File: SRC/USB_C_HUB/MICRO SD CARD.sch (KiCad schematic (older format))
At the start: 20 parts

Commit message: all but HDMI and UFP PD
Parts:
- removed J?: SD_Card, symbol Connector:SD_Card
- added J?: Micro_SD_Card_Det, symbol Connector:Micro_SD_Card_Det
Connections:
- net CRD_PWR: now also J?.4 (VDD)
- net GND: now also J?.11 (SHIELD), J?.6 (VSS)
- net SD_CD: now also J?.10 (DET_A)
- net SD_CLK: now also J?.5 (CLK)
- net SD_CMD: now also J?.3 (CMD)
- net SD_D0: now also J?.7 (DAT0)
- net SD_D1: now also J?.8 (DAT1)
- net SD_D2: now also J?.1 (DAT2)
- net SD_D3: now also J?.2 (DAT3/CD)
- net SD_WP: no longer names the net of IC?.30 (XD_D4_/_GPIO6_(SD_WP)_/_MS_SCLK)
- no-connect marks 13 -> 15
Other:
- note added: "Detect"
- moved on the sheet: C?
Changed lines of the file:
@@
 $Descr A4 11693 8268
 encoding utf-8
-Sheet 6 11
+Sheet 9 11
 Title ""
 Date ""
@@
 Comment4 ""
 $EndDescr
-Text Label 10725 3325 0    50   ~ 0
-SD_CD
 $Comp
 L OLIMEX_Power:GND #PWR?
 U 1 1 63D3BD81
-P 10775 3700
+P 10575 4100
 AR Path="/619540C6/63D3BD81" Ref="#PWR?"  Part="1"
 AR Path="/63D3BD81" Ref="#PWR?"  Part="1"
 AR Path="/63D2BAD4/63D3BD81" Ref="#PWR?"  Part="1"
 AR Path="/66525694/63D3BD81" Ref="#PWR?"  Part="1"
-F 0 "#PWR?" H 10775 3450 50  0001 C CNN
-F 1 "GND" H 10780 3527 50  0000 C CNN
-F 2 "" H 10775 3700 60  0000 C CNN
-F 3 "" H 10775 3700 60  0000 C CNN
-	1    10775 3700
+F 0 "#PWR?" H 10575 3850 50  0001 C CNN
+F 1 "GND" H 10580 3927 50  0000 C CNN
+F 2 "" H 10575 4100 60  0000 C CNN
+F 3 "" H 10575 4100 60  0000 C CNN
+	1    10575 4100
 	-1   0    0    -1
 $EndComp
 Wire Wire Line
-	10775 3625 10775 3700
-Text Label 10750 3425 0    50   ~ 0
-SD_WP
-Wire Wire Line
-	10750 3425 10550 3425
-Wire Wire Line
-	10650 3625 10775 3625
-Connection ~ 10650 3625
+	10575 4025 10575 4100
+Wire Wire Line
+	10450 4025 10575 4025
 Wire Wire Line
 	10650 3725 10650 3625
-Wire Wire Line
-	10550 3725 10650 3725
-Wire Wire Line
-	10550 3625 10650 3625
-Wire Wire Line
-	10550 3325 10725 3325
 NoConn ~ 6300 2625
 NoConn ~ 6300 2775
@@
 Wire Wire Line
 	6525 3525 6350 3525
-Text Label 6525 3525 0    50   ~ 0
-SD_WP
-Wire Wire Line
-	8050 3725 8750 3725
-Connection ~ 7800 3725
-Wire Wire Line
-	7800 3725 8050 3725
-Wire Wire Line
-	7800 3675 7800 3725
 $Comp
 L Device:C_Small C?
 U 1 1 63D332FA
-P 7800 3575
+P 7875 3625
 AR Path="/63D332FA" Ref="C?"  Part="1"
 AR Path="/63D2BAD4/63D332FA" Ref="C?"  Part="1"
 AR Path="/66525694/63D332FA" Ref="C?"  Part="1"
-F 0 "C?" H 7892 3621 50  0000 L CNN
-F 1 "1nF" H 7892 3530 50  0000 L CNN
-F 2 "" H 7800 3575 50  0001 C CNN
-F 3 "~" H 7800 3575 50  0001 C CNN
-	1    7800 3575
-	1    0    0    -1
-$EndComp
-Text Label 7800 3375 2    31   ~ 0
+F 0 "C?" H 7967 3671 50  0000 L CNN
+F 1 "1nF" H 7967 3580 50  0000 L CNN
+F 2 "" H 7875 3625 50  0001 C CNN
+F 3 "~" H 7875 3625 50  0001 C CNN
+	1    7875 3625
+	1    0    0    -1
+$EndComp
+Text Label 7875 3425 2    31   ~ 0
 CRD_PWR
-Connection ~ 8050 3725
-Wire Wire Line
-	8050 3425 8750 3425
-Wire Wire Line
-	8050 3725 8050 3425
 $Comp
 L OLIMEX_Power:GND #PWR?
 U 1 1 63D332F0
-P 7800 3725
+P 7875 3775
 AR Path="/619540C6/63D332F0" Ref="#PWR?"  Part="1"
 AR Path="/63D332F0" Ref="#PWR?"  Part="1"
 AR Path="/63D2BAD4/63D332F0" Ref="#PWR?"  Part="1"
 AR Path="/66525694/63D332F0" Ref="#PWR?"  Part="1"
-F 0 "#PWR?" H 7800 3475 50  0001 C CNN
-F 1 "GND" H 7805 3552 50  0000 C CNN
-F 2 "" H 7800 3725 60  0000 C CNN
-F 3 "" H 7800 3725 60  0000 C CNN
-	1    7800 3725
+F 0 "#PWR?" H 7875 3525 50  0001 C CNN
+F 1 "GND" H 7880 3602 50  0000 C CNN
+F 2 "" H 7875 3775 60  0000 C CNN
+F 3 "" H 7875 3775 60  0000 C CNN
+	1    7875 3775
 	-1   0    0    -1
 $EndComp
@@
 SD_CLK
 Wire Wire Line
-	8750 3625 8575 3625
-Text Label 8575 3625 2    50   ~ 0
+	8750 3525 8575 3525
+Text Label 8575 3525 2    50   ~ 0
 SD_CLK
 Wire Wire Line
@@
 SD_CMD
 Wire Wire Line
-	8575 3925 8750 3925
-Wire Wire Line
 	8575 3825 8750 3825
+Wire Wire Line
+	8575 3725 8750 3725
 Wire Wire Line
 	8575 3225 8750 3225
@@
 Text Label 8575 3125 2    50   ~ 0
 SD_D2
-Text Label 8575 3925 2    50   ~ 0
+Text Label 8575 3825 2    50   ~ 0
 SD_D1
-Text Label 8575 3825 2    50   ~ 0
+Text Label 8575 3725 2    50   ~ 0
 SD_D0
 Text Label 6525 3725 0    50   ~ 0
@@
 Text Label 6525 3325 0    50   ~ 0
 SD_D0
-$Comp
-L Connector:SD_Card J?
-U 1 1 63D332CA
-P 9650 3525
-AR Path="/63D332CA" Ref="J?"  Part="1"
-AR Path="/63D2BAD4/63D332CA" Ref="J?"  Part="1"
-AR Path="/66525694/63D332CA" Ref="J?"  Part="1"
-F 0 "J?" H 9650 4190 50  0000 C CNN
-F 1 "SD_Card" H 9650 4099 50  0000 C CNN
-F 2 "" H 9650 3525 50  0001 C CNN
-F 3 "http://portal.fciconnect.com/Comergent//fci/drawing/10067847.pdf" H 9650 3525 50  0001 C CNN
-	1    9650 3525
-	1    0    0    -1
-$EndComp
 Wire Wire Line
 	8550 2625 8900 2625
@@
 Wire Wire Line
 	2175 4050 2375 4050
+Wire Wire Line
+	7875 3425 7875 3525
+Text Label 8550 3425 2    31   ~ 0
+CRD_PWR
+Wire Wire Line
+	8750 3425 8550 3425
+Text Notes 5150 775  0    39   ~ 0
+DECOUPLING CAPS
+$Comp
+L Connector:Micro_SD_Card_Det J?
+U 1 1 66574B47
+P 9650 3525
+F 0 "J?" H 9600 4342 50  0000 C CNN
+F 1 "Micro_SD_Card_Det" H 9600 4251 50  0000 C CNN
+F 2 "" H 11700 4225 50  0001 C CNN
+F 3 "https://www.hirose.com/product/en/download_file/key_name/DM3/category/Catalog/doc_file_id/49662/?file_category_id=4&item_id=195&is_series=1" H 9650 3625 50  0001 C CNN
+	1    9650 3525
+	1    0    0    -1
+$EndComp
+Wire Wire Line
+	7875 3775 7875 3750
+Wire Wire Line
+	8750 3625 8200 3625
+Wire Wire Line
+	8200 3625 8200 3750
+Wire Wire Line
+	8200 3750 7875 3750
+Connection ~ 7875 3750
+Wire Wire Line
+	7875 3750 7875 3725
+NoConn ~ 8750 4025
 $Comp
 L SamacSys_Parts:USB2240-AEZG-06 IC?
@@
 $EndComp
 Wire Wire Line
-	7800 3375 7800 3475
-Text Label 8550 3525 2    31   ~ 0
-CRD_PWR
-Wire Wire Line
-	8750 3525 8550 3525
-Text Notes 5150 775  0    39   ~ 0
-DECOUPLING CAPS
+	10550 3625 10650 3625
+Wire Wire Line
+	10550 3725 10650 3725
+NoConn ~ 6525 3525
+Text Label 8575 3925 2    50   ~ 0
+SD_CD
+Wire Wire Line
+	8750 3925 8575 3925
+Text Notes 6825 2950 2    20   ~ 0
+Detect
 $EndSCHEMATC

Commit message: ALL DONE BUT THE HDMI SECTION. NEED FOOTPRINT ASSIGNMENT
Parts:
- removed C? (x2): 0.1uF, symbol Device:C_Small
- removed C?: 4.7uF, symbol Device:C_Small
- removed C?: 1nF, symbol Device:C_Small
- removed IC?: USB2240-AEZG-06, QFN50P600X600X100-37N-D, symbol SamacSys_Parts:USB2240-AEZG-06
- removed Y?: 24.0MHz, symbol Device:Crystal_GND24_Small
- added C69: 4.7uF, symbol Device:C_Small
- added C72, C73: 0.1uF, symbol Device:C_Small
- added C74: 1nF, symbol Device:C_Small
- added IC4: USB2240-AEZG-06, SamacSys_Parts_2:QFN50P600X600X100-37N-D, symbol SamacSys_Parts:USB2240-AEZG-06
- added Y3: 24.0MHz, symbol Device:Crystal_GND24_Small
- gave numbers to parts that had none: 14
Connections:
- net +3V3: now also C69.1, C72.1, C73.1, IC4.14 (VDD33_2), IC4.22 (VDD33_3), IC4.36 (VDDA33), IC4.6 (VDD33_1)
- net CRD_PWR: now also C74.1, IC4.21 (GPIO10_(CRD_PWR))
- net GND: now also C69.2, C72.2, C73.2, C74.2, IC4.28 (TEST), IC4.37 (GND), Y3.2, Y3.4
- net SD_CD: now also IC4.26 (GPIO15_(SD_NCD))
- net SD_CLK: now also IC4.9 (XD_NWP_/_SD_CLK_/_MS_BS)
- net SD_CMD: now also IC4.11 (XD_CLE_/_SD_CMD_/_MS_D0)
- net SD_D0: now also IC4.5 (XD_D2_/_SD_D0_/_MS_D4)
- net SD_D1: now also IC4.4 (XD_D3_/_SD_D1_/_MS_D5)
- net SD_D2: now also IC4.25 (XD_D5_/_SD_D2)
- net SD_D3: now also IC4.23 (XD_D6_/_SD_D3_/_MS_D3)
- net USB+: now also IC4.2 (USB+)
- net USB-: now also IC4.3 (USB-)
- net XTAL1: now also IC4.33 (XTAL1_(CLKIN)), Y3.1
- net XTAL2: now also IC4.32 (XTAL2), Y3.3
- net at R56.2: now also IC4.18 (RESET_N)
- net at C67.1: now also IC4.34 (VDD18PLL)
- net at C68.1: now also IC4.13 (VDD18)
- net at R57.1: now also IC4.35 (RBIAS)
- net at R58.2: now also IC4.29 (GPIO4)

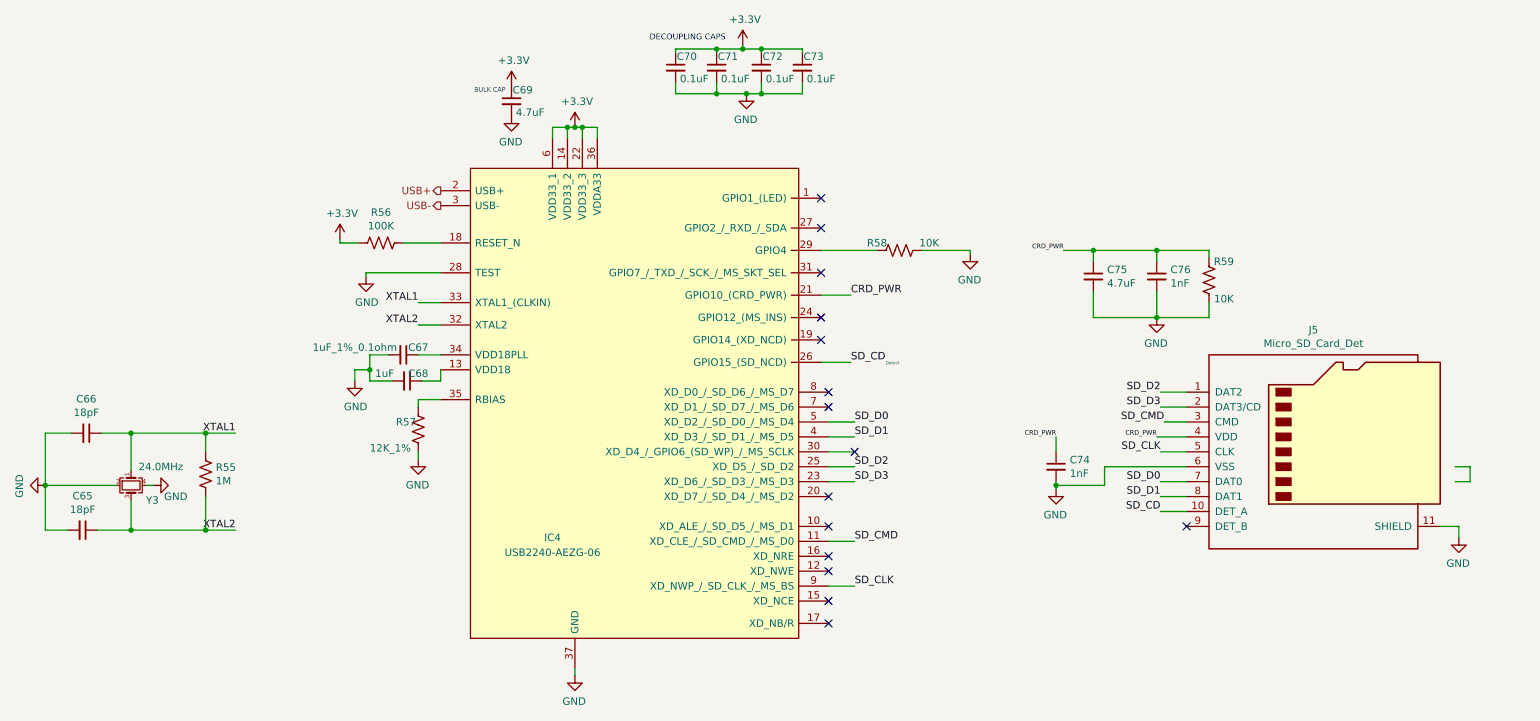
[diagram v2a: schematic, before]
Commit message: schematic capture complete. Pending Footprint assignment. accetable Errors=21
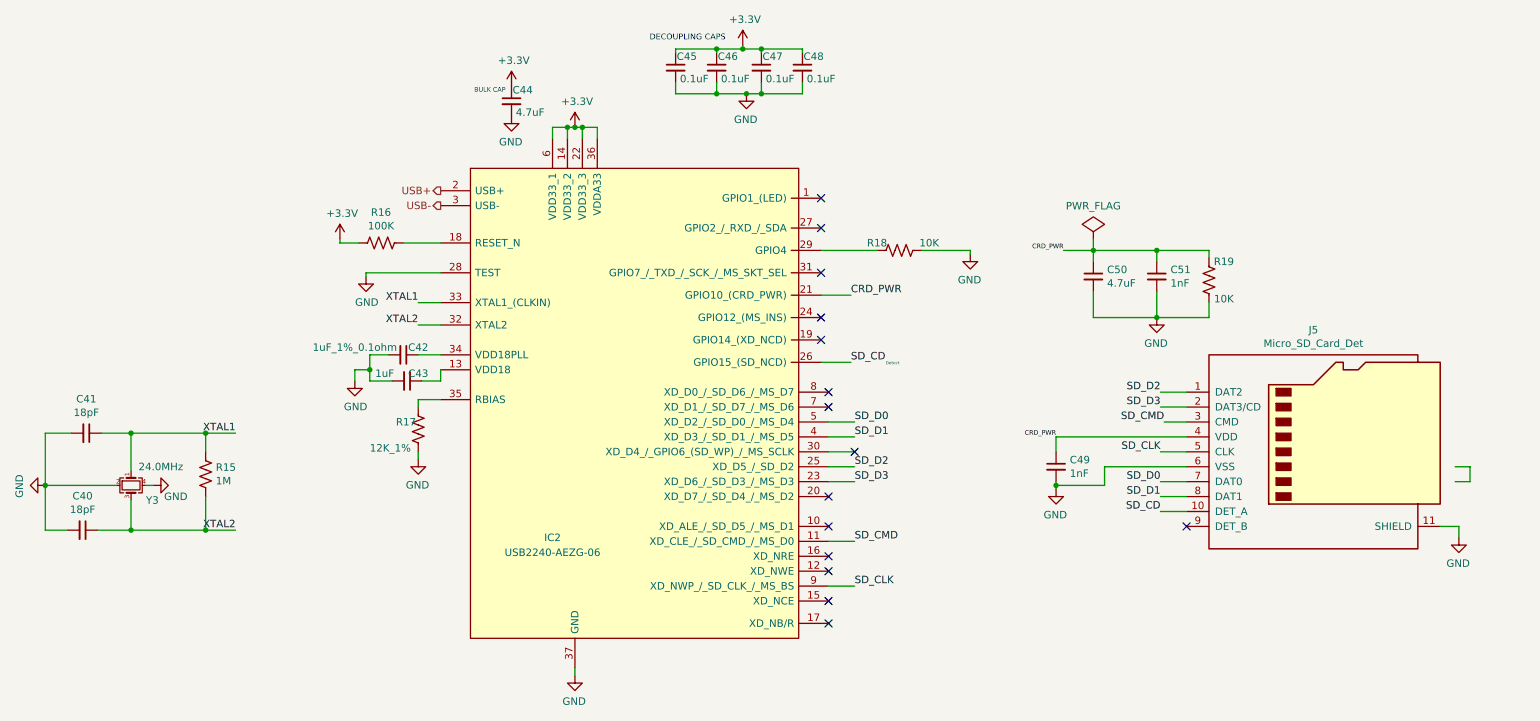
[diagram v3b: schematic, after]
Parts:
- renumbered C65 to C40, C66 to C41, C67 to C42, C68 to C43, C69 to C44, C70 to C45, C71 to C46, C72 to C47, C73 to C48, C74 to C49, C75 to C50, C76 to C51, IC4 to IC2, R55 to R15, R56 to R16, R57 to R17, R58 to R18, R59 to R19

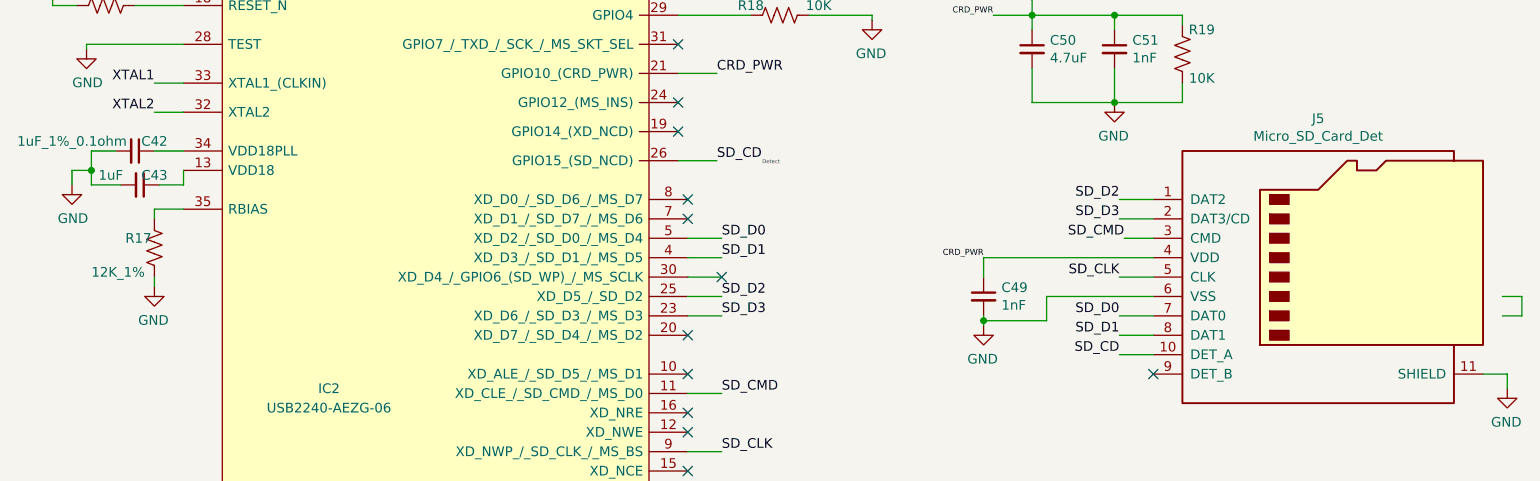
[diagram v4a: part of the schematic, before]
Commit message: schematic capture and footprint assignment complete. Pending approval
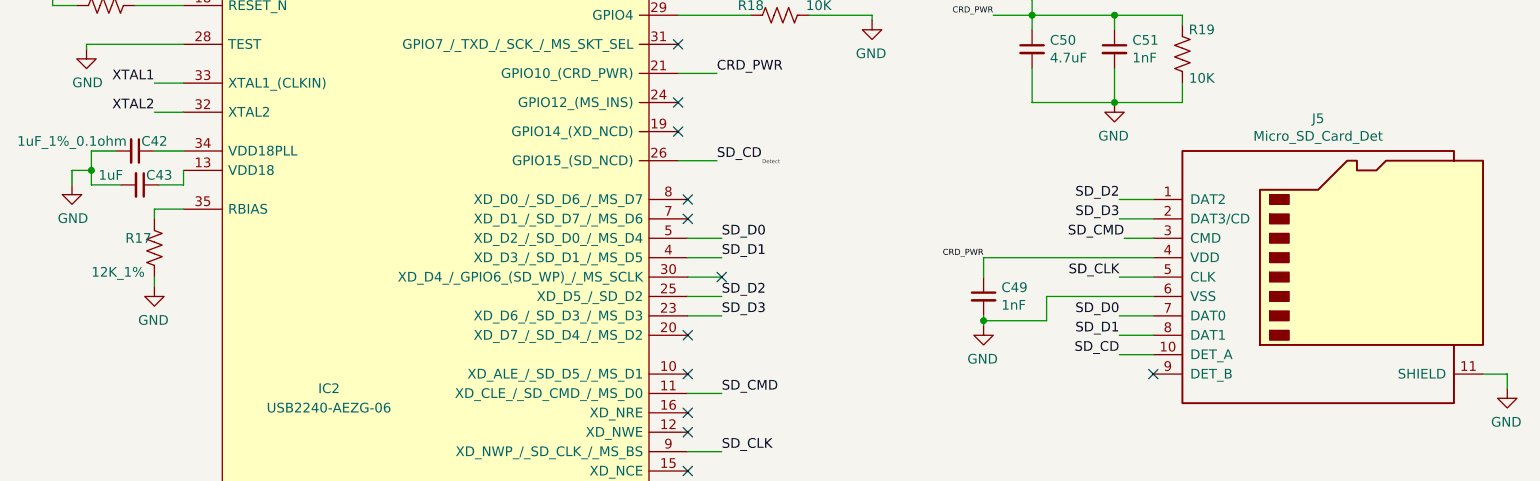
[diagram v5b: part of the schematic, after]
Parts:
- C40, C41, C45, C46, C47, C48: footprint (none) -> Capacitor_SMD:C_0402_1005Metric
- C42, C43: footprint (none) -> Capacitor_SMD:C_0603_1608Metric; Mfr No. (none) -> GMC10X7R105J16NT; Vendor (none) -> DK
- C44, C50: footprint (none) -> Capacitor_SMD:C_0603_1608Metric; Mfr No. (none) -> CL10A475KQ8NNNC
- C49, C51: footprint (none) -> Capacitor_SMD:C_0402_1005Metric; Mfr No. (none) -> C0402C102J1GEC7411
- J5: footprint (none) -> footprints:GCT_MEM2051-00-195-00-A
- R15, R18, R19: footprint (none) -> Resistor_SMD:R_0402_1005Metric
- R16: footprint (none) -> Resistor_SMD:R_0402_1005Metric; Mfr No. (none) -> 0402WGF1003TCE
- R17: footprint (none) -> Resistor_SMD:R_0402_1005Metric; Mfr No. (none) -> RTT021202FTH
- Y3: footprint (none) -> Crystal:Crystal_SMD_2016-4Pin_2.0x1.6mm; Mfr No. (none) -> ABM11-24.000MHZ-D2X-T3
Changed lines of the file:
@@
 Wire Wire Line
 	10450 4025 10575 4025
-Wire Wire Line
-	10650 3725 10650 3625
 NoConn ~ 6300 2625
 NoConn ~ 6300 2775
@@
 F 0 "C49" H 7967 3671 50  0000 L CNN
 F 1 "1nF" H 7967 3580 50  0000 L CNN
-F 2 "" H 7875 3625 50  0001 C CNN
+F 2 "Capacitor_SMD:C_0402_1005Metric" H 7875 3625 50  0001 C CNN
 F 3 "~" H 7875 3625 50  0001 C CNN
+F 4 "C0402C102J1GEC7411" H 7875 3625 50  0001 C CNN "Mfr No."
 	1    7875 3625
 	1    0    0    -1
@@
 F 0 "R19" H 8800 2250 50  0000 C CNN
 F 1 "10K" H 8800 2500 50  0000 C CNN
-F 2 "" V 8940 2365 50  0001 C CNN
+F 2 "Resistor_SMD:R_0402_1005Metric" V 8940 2365 50  0001 C CNN
 F 3 "~" H 8900 2375 50  0001 C CNN
 	1    8900 2375
@@
 F 0 "C51" H 8642 2396 50  0000 L CNN
 F 1 "1nF" H 8642 2305 50  0000 L CNN
-F 2 "" H 8550 2350 50  0001 C CNN
+F 2 "Capacitor_SMD:C_0402_1005Metric" H 8550 2350 50  0001 C CNN
 F 3 "~" H 8550 2350 50  0001 C CNN
+F 4 "C0402C102J1GEC7411" H 8550 2350 50  0001 C CNN "Mfr No."
 	1    8550 2350
 	1    0    0    -1
@@
 F 0 "C50" H 8217 2396 50  0000 L CNN
 F 1 "4.7uF" H 8217 2305 50  0000 L CNN
-F 2 "" H 8125 2350 50  0001 C CNN
+F 2 "Capacitor_SMD:C_0603_1608Metric" H 8125 2350 50  0001 C CNN
 F 3 "~" H 8125 2350 50  0001 C CNN
+F 4 "CL10A475KQ8NNNC" H 8125 2350 50  0001 C CNN "Mfr No."
 	1    8125 2350
 	1    0    0    -1
@@
 F 0 "R18" V 6775 2025 50  0000 C CNN
 F 1 "10K" V 6775 2375 50  0000 C CNN
-F 2 "" V 6865 2165 50  0001 C CNN
+F 2 "Resistor_SMD:R_0402_1005Metric" V 6865 2165 50  0001 C CNN
 F 3 "~" H 6825 2175 50  0001 C CNN
 	1    6825 2175
@@
 F 0 "R17" H 3450 3425 50  0000 L CNN
 F 1 "12K_1%" H 3275 3250 50  0000 L CNN
-F 2 "" V 3640 3365 50  0001 C CNN
+F 2 "Resistor_SMD:R_0402_1005Metric" V 3640 3365 50  0001 C CNN
 F 3 "~" H 3600 3375 50  0001 C CNN
+F 4 "RTT021202FTH" H 3600 3375 50  0001 C CNN "Mfr No."
 	1    3600 3375
 	1    0    0    -1
@@
 AR Path="/63D2BAD4/642D7819" Ref="C?"  Part="1"
 AR Path="/66525694/642D7819" Ref="C44"  Part="1"
+AR Path="/6609E24E/642D7819" Ref="C44"  Part="1"
 F 0 "C44" H 4300 1250 50  0000 C CNN
 F 1 "4.7uF" H 4350 1100 50  0000 C CNN
-F 2 "" H 4225 1175 50  0001 C CNN
+F 2 "Capacitor_SMD:C_0603_1608Metric" H 4225 1175 50  0001 C CNN
 F 3 "~" H 4225 1175 50  0001 C CNN
+F 4 "CL10A475KQ8NNNC" H 4225 1175 50  0001 C CNN "Mfr No."
 	1    4225 1175
 	1    0    0    -1
@@
 F 0 "C48" H 6250 1025 50  0000 C CNN
 F 1 "0.1uF" H 6300 875 50  0000 C CNN
-F 2 "" H 6175 950 50  0001 C CNN
+F 2 "Capacitor_SMD:C_0402_1005Metric" H 6175 950 50  0001 C CNN
 F 3 "~" H 6175 950 50  0001 C CNN
 	1    6175 950
@@
 F 0 "C47" H 5975 1025 50  0000 C CNN
 F 1 "0.1uF" H 6025 875 50  0000 C CNN
-F 2 "" H 5900 950 50  0001 C CNN
+F 2 "Capacitor_SMD:C_0402_1005Metric" H 5900 950 50  0001 C CNN
 F 3 "~" H 5900 950 50  0001 C CNN
 	1    5900 950
@@
 F 0 "C46" H 5675 1025 50  0000 C CNN
 F 1 "0.1uF" H 5725 875 50  0000 C CNN
-F 2 "" H 5600 950 50  0001 C CNN
+F 2 "Capacitor_SMD:C_0402_1005Metric" H 5600 950 50  0001 C CNN
 F 3 "~" H 5600 950 50  0001 C CNN
 	1    5600 950
@@
 F 0 "C45" H 5400 1025 50  0000 C CNN
 F 1 "0.1uF" H 5450 875 50  0000 C CNN
-F 2 "" H 5325 950 50  0001 C CNN
+F 2 "Capacitor_SMD:C_0402_1005Metric" H 5325 950 50  0001 C CNN
 F 3 "~" H 5325 950 50  0001 C CNN
 	1    5325 950
@@
 AR Path="/63D2BAD4/63D33216" Ref="C?"  Part="1"
 AR Path="/66525694/63D33216" Ref="C43"  Part="1"
-F 0 "C43" V 3475 3125 50  0000 C CNN
+F 0 "C43" V 3475 3150 50  0000 C CNN
 F 1 "1uF" V 3475 2900 50  0000 C CNN
-F 2 "" H 3525 3050 50  0001 C CNN
+F 2 "Capacitor_SMD:C_0603_1608Metric" H 3525 3050 50  0001 C CNN
 F 3 "~" H 3525 3050 50  0001 C CNN
+F 4 "GMC10X7R105J16NT" V 3525 3050 50  0001 C CNN "Mfr No."
+F 5 "DK" V 3525 3050 50  0001 C CNN "Vendor"
 	1    3525 3050
 	0    1    1    0
@@
 P 3500 2875
 AR Path="/63D3320A" Ref="C?"  Part="1"
-AR Path="/63D2BAD4/63D3320A" Ref="C?"  Part="1"
+AR Path="/63D2BAD4/63D3320A" Ref="C42"  Part="1"
 AR Path="/66525694/63D3320A" Ref="C42"  Part="1"
 F 0 "C42" V 3450 2975 50  0000 C CNN
 F 1 "1uF_1%_0.1ohm" V 3450 2550 50  0000 C CNN
-F 2 "" H 3500 2875 50  0001 C CNN
+F 2 "Capacitor_SMD:C_0603_1608Metric" H 3500 2875 50  0001 C CNN
 F 3 "~" H 3500 2875 50  0001 C CNN
+F 4 "GMC10X7R105J16NT" V 3500 2875 50  0001 C CNN "Mfr No."
+F 5 "DK" V 3500 2875 50  0001 C CNN "Vendor"
 	1    3500 2875
 	0    1    1    0
@@
 F 0 "R16" V 3555 2125 50  0000 C CNN
 F 1 "100K" V 3464 2125 50  0000 C CNN
-F 2 "" V 3390 2115 50  0001 C CNN
+F 2 "Resistor_SMD:R_0402_1005Metric" V 3390 2115 50  0001 C CNN
 F 3 "~" H 3350 2125 50  0001 C CNN
+F 4 "0402WGF1003TCE" V 3350 2125 50  0001 C CNN "Mfr No."
 	1    3350 2125
 	0    -1   -1   0
@@
 F 0 "Y3" V 1775 3850 50  0000 L CNN
 F 1 "24.0MHz" V 1550 3800 50  0000 L CNN
-F 2 "" H 1675 3750 50  0001 C CNN
+F 2 "Crystal:Crystal_SMD_2016-4Pin_2.0x1.6mm" H 1675 3750 50  0001 C CNN
 F 3 "~" H 1675 3750 50  0001 C CNN
+F 4 "ABM11-24.000MHZ-D2X-T3" V 1675 3750 50  0001 C CNN "Mfr No."
 	1    1675 3750
 	0    1    1    0
@@
 F 0 "C41" V 1146 3400 50  0000 C CNN
 F 1 "18pF" V 1237 3400 50  0000 C CNN
-F 2 "" H 1375 3400 50  0001 C CNN
+F 2 "Capacitor_SMD:C_0402_1005Metric" H 1375 3400 50  0001 C CNN
 F 3 "~" H 1375 3400 50  0001 C CNN
 	1    1375 3400
@@
 F 0 "C40" V 1121 4050 50  0000 C CNN
 F 1 "18pF" V 1212 4050 50  0000 C CNN
-F 2 "" H 1350 4050 50  0001 C CNN
+F 2 "Capacitor_SMD:C_0402_1005Metric" H 1350 4050 50  0001 C CNN
 F 3 "~" H 1350 4050 50  0001 C CNN
 	1    1350 4050
@@
 F 0 "R15" H 2243 3721 50  0000 L CNN
 F 1 "1M" H 2243 3630 50  0000 L CNN
-F 2 "" V 2215 3665 50  0001 C CNN
+F 2 "Resistor_SMD:R_0402_1005Metric" V 2215 3665 50  0001 C CNN
 F 3 "~" H 2175 3675 50  0001 C CNN
 	1    2175 3675
@@
 F 0 "J5" H 9600 4342 50  0000 C CNN
 F 1 "Micro_SD_Card_Det" H 9600 4251 50  0000 C CNN
-F 2 "" H 11700 4225 50  0001 C CNN
+F 2 "footprints:GCT_MEM2051-00-195-00-A" H 11700 4225 50  0001 C CNN
 F 3 "https://www.hirose.com/product/en/download_file/key_name/DM3/category/Catalog/doc_file_id/49662/?file_category_id=4&item_id=195&is_series=1" H 9650 3625 50  0001 C CNN
 	1    9650 3525
@@
 	1    0    0    -1
 $EndComp
-Wire Wire Line
-	10550 3625 10650 3625
-Wire Wire Line
-	10550 3725 10650 3725
 NoConn ~ 6525 3525
 Text Label 8575 3925 2    50   ~ 0
